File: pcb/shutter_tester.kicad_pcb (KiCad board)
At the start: 2 copper layers, 53 x 42 mm, 24 parts, among them J1 Conn_01x02, J2 Conn_01x02, J3 Conn_01x02, J4 Conn_01x02, Q1 MMBTA13LT3G, Q2 MMBTA13LT3G, Q3 MMBTA13LT3G, Q4 MMBTA13LT3G

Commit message: change to single light sensor
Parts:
- removed D2, D3, D4: LED, LED_THT:LED_D3.0mm
- removed J2, J3, J4: Conn_01x02, Connector_PinHeader_2.54mm:PinHeader_1x02_P2.54mm_Horizontal
- removed JP1, JP2, JP3: 0R, Resistor_SMD:R_1206_3216Metric
- removed Q2, Q3, Q4: MMBTA13LT3G, Package_TO_SOT_SMD:SOT-23
- removed R2, R3, R4: 2k, Resistor_SMD:R_0805_2012Metric_Pad1.20x1.40mm_HandSolder
- moved J1 25.8 mm to (135.6, 113.5), turned to 180 degrees
- moved R1 20.6 mm to (157.5, 117.8), turned to 180 degrees
- moved D1 17.8 mm to (158.8, 122.0), turned to 180 degrees
- moved Q1 16.4 mm to (152.3, 121.0)
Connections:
- J1 pad 1: Net-(J1-Pad1) -> GND
- J1 pad 2: GND -> Net-(J1-Pad2)
- Q1 pad 1: Net-(JP1-Pad1) -> Net-(D1-Pad2)
- Q1 pad 3: Net-(J1-Pad1) -> Net-(J1-Pad2)
- R1 pad 2: Net-(J1-Pad1) -> Net-(J1-Pad2)
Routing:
- net VCC: track 104.1 -> 28.1 mm
- net Net-(J1-Pad2): track 0.00 -> 29.7 mm
- net Net-(D3-Pad2): track 23.2 -> 0.00 mm
- net Net-(J4-Pad1): track 20.2 -> 0.00 mm
- net Net-(J3-Pad1): track 20.0 -> 0.00 mm
- net Net-(JP2-Pad1): track 10.3 -> 0.00 mm
- net Net-(J2-Pad1): track 8.12 -> 0.00 mm
- net Net-(J1-Pad1): track 8.12 -> 0.00 mm
- net Net-(JP1-Pad1): track 6.10 -> 0.00 mm
- net Net-(JP3-Pad1): track 4.83 -> 0.00 mm
- net Net-(D4-Pad2): track 4.41 -> 0.00 mm
- net Net-(D2-Pad2): track 4.23 -> 0.00 mm
- net Net-(D1-Pad2): track 5.16 -> 2.98 mm

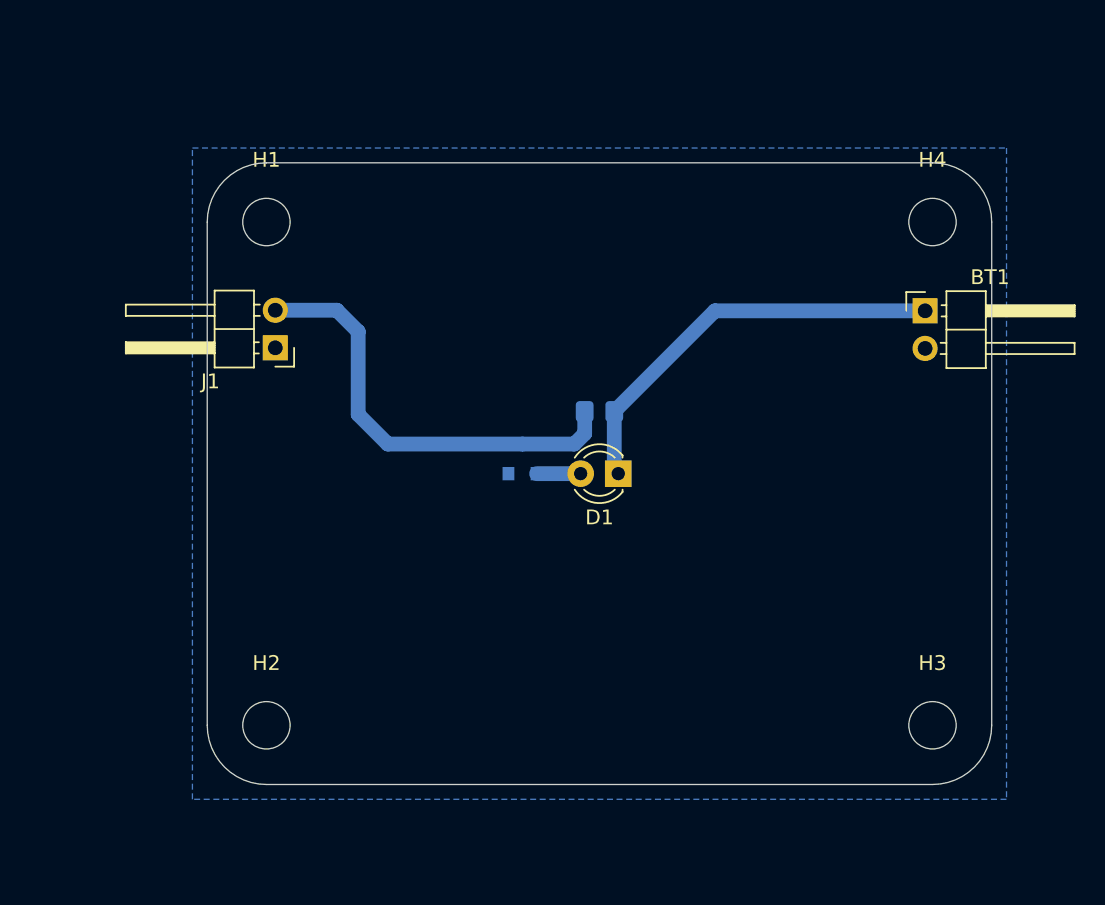
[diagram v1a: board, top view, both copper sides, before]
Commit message: add comparator circuit
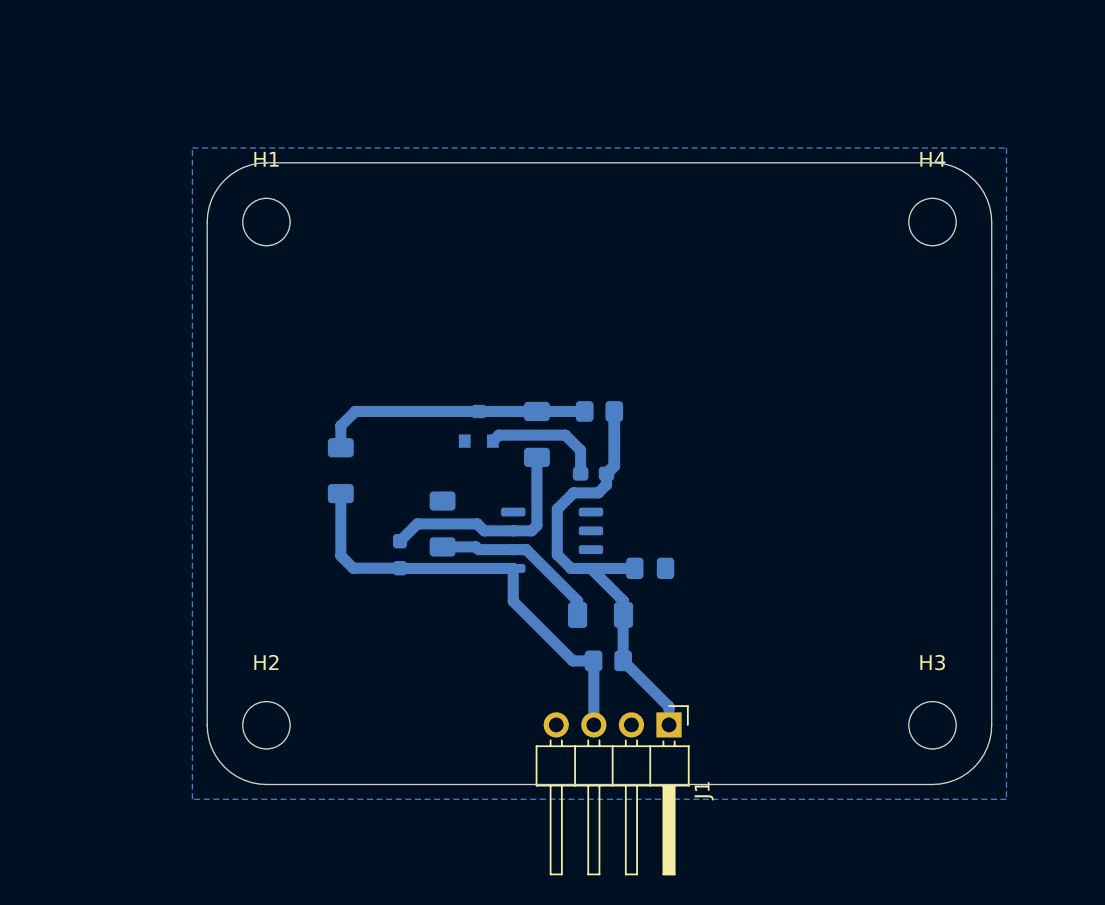
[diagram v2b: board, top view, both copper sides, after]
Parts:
- removed BT1: 2x AA, Connector_PinHeader_2.54mm:PinHeader_1x02_P2.54mm_Horizontal
- added C1: 100n, Capacitor_SMD:C_0805_2012Metric_Pad1.18x1.45mm_HandSolder, B.Cu at (160.9, 128.4)
- added JP1: Comparitor Bypass, Resistor_SMD:R_1206_3216Metric_Pad1.30x1.75mm_HandSolder, B.Cu at (140.0, 121.8)
- added R2: 10k, Resistor_SMD:R_1206_3216Metric_Pad1.30x1.75mm_HandSolder, B.Cu at (153.3, 119.3)
- added R3: 10k, Resistor_SMD:R_1206_3216Metric_Pad1.30x1.75mm_HandSolder, B.Cu at (157.6, 131.6)
- added R4: 10k, Resistor_SMD:R_1206_3216Metric_Pad1.30x1.75mm_HandSolder, B.Cu at (146.9, 125.4)
- added R5: 4.7M, Resistor_SMD:R_0603_1608Metric_Pad0.98x0.95mm_HandSolder, B.Cu at (144.0, 127.5)
- added R6: 3k, Resistor_SMD:R_0805_2012Metric_Pad1.20x1.40mm_HandSolder, B.Cu at (158.1, 134.7)
- added U1: LM393, Package_SO:SOP-8_3.9x4.9mm_P1.27mm, B.Cu at (154.3, 126.5)
- D1: footprint LED_THT:LED_D3.0mm -> LED_SMD:LED_0603_1608Metric_Pad1.05x0.95mm_HandSolder; moved to B.Cu
- J1: value Conn_01x02 -> Conn_01x04; footprint Connector_PinHeader_2.54mm:PinHeader_1x02_P2.54mm_Horizontal -> Connector_PinHeader_2.54mm:PinHeader_1x04_P2.54mm_Horizontal
- moved J1 36.8 mm to (162.2, 139.0), turned to 270 degrees
- moved Q1 3.68 mm to (149.3, 118.8)
- moved D1 1.67 mm to (157.1, 122.0)
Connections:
- J1 pad 1: GND -> VCC
- J1 pad 2: Net-(J1-Pad2) -> GND
- Q1 pad 3: Net-(J1-Pad2) -> Net-(JP1-Pad1)
- R1 pad 2: Net-(J1-Pad2) -> Net-(JP1-Pad1)
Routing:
- net /OUTPUT: track 0.00 -> 29.8 mm
- net Net-(J1-Pad2): track 29.7 -> 0.00 mm
- net Net-(JP1-Pad1): track 0.00 -> 18.4 mm
- net Net-(R2-Pad1): track 0.00 -> 14.7 mm
- net Net-(R3-Pad1): track 0.00 -> 11.6 mm
- net Net-(D1-Pad2): track 2.98 -> 8.09 mm
- net VCC: track 28.1 -> 30.7 mm

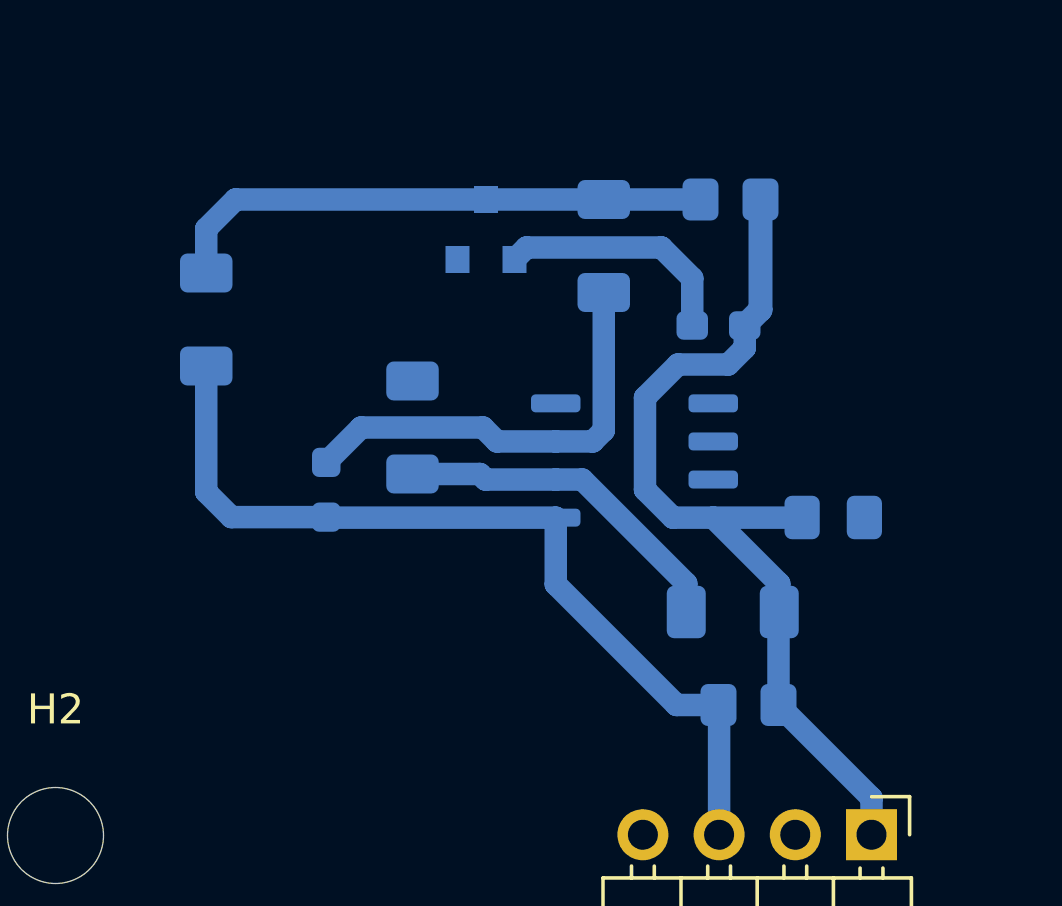
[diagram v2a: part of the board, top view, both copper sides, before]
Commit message: move tracks for engraving tip access
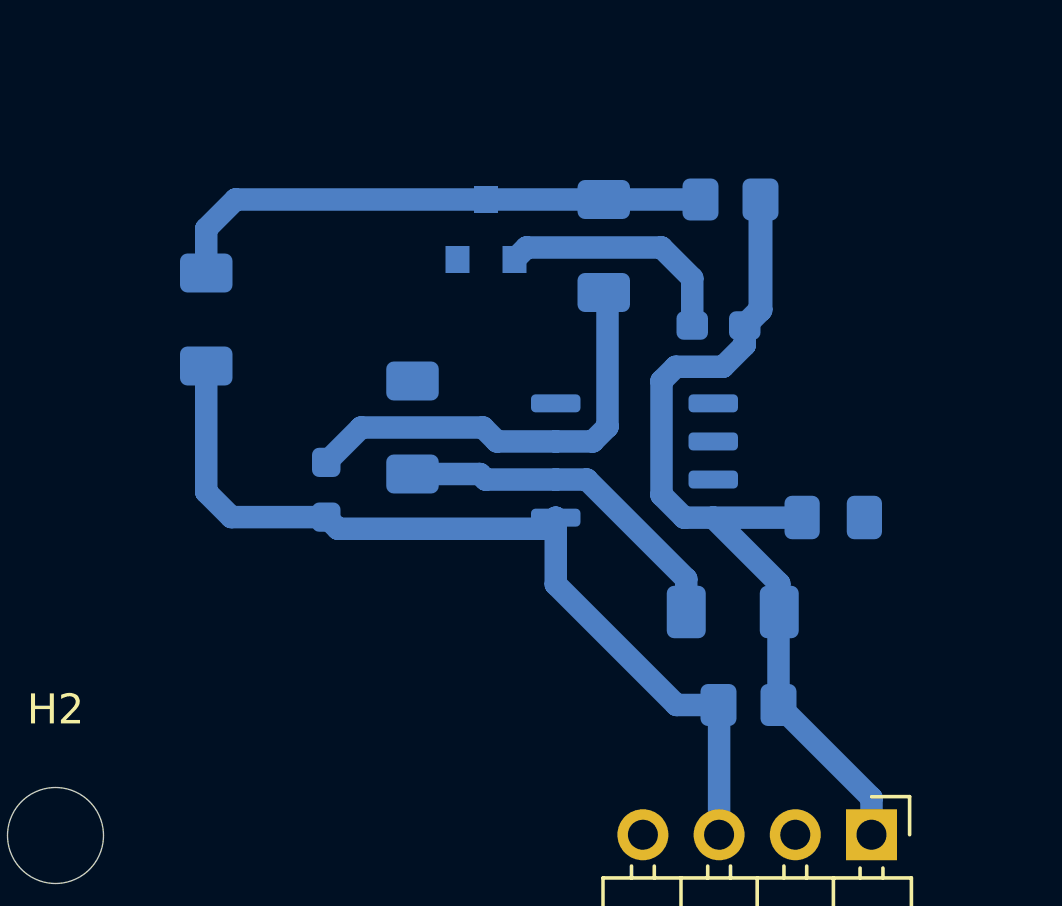
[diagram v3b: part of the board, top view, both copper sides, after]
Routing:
- net VCC: track 30.7 -> 29.9 mm
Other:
- net class Default: clearance 0.2 -> 0.4536
- rule trace_clearance: 0.2 -> 0.4536
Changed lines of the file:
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@@
     (thickness 1.6)
     (drawings 12)
-    (tracks 51)
+    (tracks 53)
     (zones 0)
     (modules 16)
@@
     (user_trace_width 0.8)
     (user_trace_width 1)
-    (trace_clearance 0.2)
+    (trace_clearance 0.4536)
     (zone_clearance 0.508)
     (zone_45_only yes)
@@
   (net 7 /OUTPUT)
   (net_class Default "This is the default net class."
-    (clearance 0.2)
+    (clearance 0.4536)
     (trace_width 0.25)
     (via_dia 0.8)
@@
     (fp_line (start 2.45 1.12) (end 2.45 -1.12) (layer B.CrtYd) (width 0.05))
     (fp_line (start 2.45 -1.12) (end -2.45 -1.12) (layer B.CrtYd) (width 0.05))
-    (pad 2 smd roundrect (at 1.55 0 270) (size 1.3 1.75) (layers B.Cu B.Paste B.Mask) (roundrect_rratio 0.192308)
+    (pad 2 smd roundrect (at 1.55 0 270) (size 1.3 1.75) (layers B.Cu B.Paste B.Mask) (roundrect_rratio 0.1923076923076923)
       (net 7 /OUTPUT))
-    (pad 1 smd roundrect (at -1.55 0 270) (size 1.3 1.75) (layers B.Cu B.Paste B.Mask) (roundrect_rratio 0.192308)
+    (pad 1 smd roundrect (at -1.55 0 270) (size 1.3 1.75) (layers B.Cu B.Paste B.Mask) (roundrect_rratio 0.1923076923076923)
       (net 4 "Net-(JP1-Pad1)"))
     (model ${KISYS3DMOD}/Resistor_SMD.3dshapes/R_1206_3216Metric.wrl
@@
     (fp_line (start 2.45 1.12) (end 2.45 -1.12) (layer B.CrtYd) (width 0.05))
     (fp_line (start 2.45 -1.12) (end -2.45 -1.12) (layer B.CrtYd) (width 0.05))
-    (pad 2 smd roundrect (at 1.55 0 90) (size 1.3 1.75) (layers B.Cu B.Paste B.Mask) (roundrect_rratio 0.192308)
+    (pad 2 smd roundrect (at 1.55 0 90) (size 1.3 1.75) (layers B.Cu B.Paste B.Mask) (roundrect_rratio 0.1923076923076923)
       (net 4 "Net-(JP1-Pad1)"))
-    (pad 1 smd roundrect (at -1.55 0 90) (size 1.3 1.75) (layers B.Cu B.Paste B.Mask) (roundrect_rratio 0.192308)
+    (pad 1 smd roundrect (at -1.55 0 90) (size 1.3 1.75) (layers B.Cu B.Paste B.Mask) (roundrect_rratio 0.1923076923076923)
       (net 5 "Net-(R2-Pad1)"))
     (model ${KISYS3DMOD}/Resistor_SMD.3dshapes/R_1206_3216Metric.wrl
@@
       (effects (font (size 0.8 0.8) (thickness 0.12)) (justify mirror))
     )
-    (pad 2 smd roundrect (at 1.55 0 270) (size 1.3 1.75) (layers B.Cu B.Paste B.Mask) (roundrect_rratio 0.192308)
+    (pad 2 smd roundrect (at 1.55 0 270) (size 1.3 1.75) (layers B.Cu B.Paste B.Mask) (roundrect_rratio 0.1923076923076923)
       (net 6 "Net-(R3-Pad1)"))
-    (pad 1 smd roundrect (at -1.55 0 270) (size 1.3 1.75) (layers B.Cu B.Paste B.Mask) (roundrect_rratio 0.192308)
+    (pad 1 smd roundrect (at -1.55 0 270) (size 1.3 1.75) (layers B.Cu B.Paste B.Mask) (roundrect_rratio 0.1923076923076923)
       (net 1 GND))
     (model ${KISYS3DMOD}/Resistor_SMD.3dshapes/R_1206_3216Metric.wrl
@@
       (effects (font (size 0.8 0.8) (thickness 0.12)) (justify mirror))
     )
-    (pad 2 smd roundrect (at 1.55 0) (size 1.3 1.75) (layers B.Cu B.Paste B.Mask) (roundrect_rratio 0.192308)
+    (pad 2 smd roundrect (at 1.55 0) (size 1.3 1.75) (layers B.Cu B.Paste B.Mask) (roundrect_rratio 0.1923076923076923)
       (net 2 VCC))
-    (pad 1 smd roundrect (at -1.55 0) (size 1.3 1.75) (layers B.Cu B.Paste B.Mask) (roundrect_rratio 0.192308)
+    (pad 1 smd roundrect (at -1.55 0) (size 1.3 1.75) (layers B.Cu B.Paste B.Mask) (roundrect_rratio 0.1923076923076923)
       (net 6 "Net-(R3-Pad1)"))
     (model ${KISYS3DMOD}/Resistor_SMD.3dshapes/R_1206_3216Metric.wrl
@@
       (effects (font (size 0.5 0.5) (thickness 0.08)) (justify mirror))
     )
-    (pad 2 smd roundrect (at 1.0375 0) (size 1.175 1.45) (layers B.Cu B.Paste B.Mask) (roundrect_rratio 0.212766)
-      (net 1 GND))
-    (pad 1 smd roundrect (at -1.0375 0) (size 1.175 1.45) (layers B.Cu B.Paste B.Mask) (roundrect_rratio 0.212766)
+    (pad 2 smd roundrect (at 1.0375 0) (size 1.175 1.45) (layers B.Cu B.Paste B.Mask) (roundrect_rratio 0.2127659574468085)
+      (net 1 GND))
+    (pad 1 smd roundrect (at -1.0375 0) (size 1.175 1.45) (layers B.Cu B.Paste B.Mask) (roundrect_rratio 0.2127659574468085)
       (net 2 VCC))
     (model ${KISYS3DMOD}/Capacitor_SMD.3dshapes/C_0805_2012Metric.wrl
@@
       (effects (font (size 0.5 0.5) (thickness 0.08)) (justify mirror))
     )
-    (pad 2 smd roundrect (at 1 0) (size 1.2 1.4) (layers B.Cu B.Paste B.Mask) (roundrect_rratio 0.208333)
+    (pad 2 smd roundrect (at 1 0) (size 1.2 1.4) (layers B.Cu B.Paste B.Mask) (roundrect_rratio 0.2083325)
       (net 2 VCC))
-    (pad 1 smd roundrect (at -1 0) (size 1.2 1.4) (layers B.Cu B.Paste B.Mask) (roundrect_rratio 0.208333)
+    (pad 1 smd roundrect (at -1 0) (size 1.2 1.4) (layers B.Cu B.Paste B.Mask) (roundrect_rratio 0.2083325)
       (net 7 /OUTPUT))
     (model ${KISYS3DMOD}/Resistor_SMD.3dshapes/R_0805_2012Metric.wrl
@@
   (segment (start 159.8825 128.405) (end 159.8875 128.4) (width 0.75) (layer B.Cu) (net 2))
   (segment (start 156.925 128.405) (end 159.8825 128.405) (width 0.75) (layer B.Cu) (net 2))
-  (segment (start 157.975 122.75) (end 157.975 122) (width 0.75) (layer B.Cu) (net 2))
-  (segment (start 157.425 123.3) (end 157.975 122.75) (width 0.75) (layer B.Cu) (net 2))
-  (segment (start 154.65 124.4) (end 155.75 123.3) (width 0.75) (layer B.Cu) (net 2))
-  (segment (start 154.65 127.475) (end 154.65 124.4) (width 0.75) (layer B.Cu) (net 2))
-  (segment (start 155.75 123.3) (end 157.425 123.3) (width 0.75) (layer B.Cu) (net 2))
-  (segment (start 155.58 128.405) (end 154.65 127.475) (width 0.75) (layer B.Cu) (net 2))
-  (segment (start 156.925 128.405) (end 155.58 128.405) (width 0.75) (layer B.Cu) (net 2))
   (segment (start 162.2 137.75) (end 159.1 134.65) (width 0.75) (layer B.Cu) (net 2))
   (segment (start 162.2 138.975) (end 162.2 137.75) (width 0.75) (layer B.Cu) (net 2))
@@
   (segment (start 159.125 130.605) (end 156.925 128.405) (width 0.75) (layer B.Cu) (net 2))
   (segment (start 159.125 131.55) (end 159.125 130.605) (width 0.75) (layer B.Cu) (net 2))
+  (segment (start 157.25 123.375) (end 157.975 122.65) (width 0.75) (layer B.Cu) (net 2))
+  (segment (start 155.675 123.375) (end 157.25 123.375) (width 0.75) (layer B.Cu) (net 2))
+  (segment (start 155.2 123.85) (end 155.675 123.375) (width 0.75) (layer B.Cu) (net 2))
+  (segment (start 155.2 127.65) (end 155.2 123.85) (width 0.75) (layer B.Cu) (net 2))
+  (segment (start 155.955 128.405) (end 155.2 127.65) (width 0.75) (layer B.Cu) (net 2))
+  (segment (start 157.975 122.65) (end 157.975 122) (width 0.75) (layer B.Cu) (net 2))
+  (segment (start 156.925 128.405) (end 155.955 128.405) (width 0.75) (layer B.Cu) (net 2))
   (segment (start 156.225 122) (end 156.225 120.425) (width 0.75) (layer B.Cu) (net 3))
   (segment (start 156.225 120.425) (end 155.2 119.4) (width 0.75) (layer B.Cu) (net 3))
   (segment (start 150.7 119.4) (end 150.3 119.8) (width 0.75) (layer B.Cu) (net 3))
   (segment (start 155.2 119.4) (end 150.7 119.4) (width 0.75) (layer B.Cu) (net 3))
-  (segment (start 151.675 125.865) (end 152.91 125.865) (width 0.75) (layer B.Cu) (net 5))
-  (segment (start 153.275 125.5) (end 153.275 120.9) (width 0.75) (layer B.Cu) (net 5))
-  (segment (start 152.91 125.865) (end 153.275 125.5) (width 0.75) (layer B.Cu) (net 5))
-  (segment (start 144.0425 128.405) (end 144.025 128.3875) (width 0.75) (layer B.Cu) (net 7))
-  (segment (start 151.675 128.405) (end 144.0425 128.405) (width 0.75) (layer B.Cu) (net 7))
   (segment (start 157.12 134.67) (end 157.1 134.65) (width 0.75) (layer B.Cu) (net 7))
   (segment (start 157.12 138.975) (end 157.12 134.67) (width 0.75) (layer B.Cu) (net 7))
@@
   (segment (start 145.1875 125.4) (end 149.25 125.4) (width 0.75) (layer B.Cu) (net 5))
   (segment (start 144.025 126.5625) (end 145.1875 125.4) (width 0.75) (layer B.Cu) (net 5))
+  (segment (start 153.4 121.025) (end 153.275 120.9) (width 0.75) (layer B.Cu) (net 5))
+  (segment (start 153.4 125.375) (end 153.4 121.025) (width 0.75) (layer B.Cu) (net 5))
+  (segment (start 152.91 125.865) (end 153.4 125.375) (width 0.75) (layer B.Cu) (net 5))
+  (segment (start 151.675 125.865) (end 152.91 125.865) (width 0.75) (layer B.Cu) (net 5))
   (segment (start 151.675 127.135) (end 149.335 127.135) (width 0.75) (layer B.Cu) (net 6))
   (segment (start 149.15 126.95) (end 146.9 126.95) (width 0.75) (layer B.Cu) (net 6))
   (segment (start 149.335 127.135) (end 149.15 126.95) (width 0.75) (layer B.Cu) (net 6))
   (segment (start 156.025 131.475) (end 156.025 131.55) (width 0.75) (layer B.Cu) (net 6))
-  (segment (start 156.025 130.6) (end 156.025 131.475) (width 0.75) (layer B.Cu) (net 6))
-  (segment (start 152.56 127.135) (end 156.025 130.6) (width 0.75) (layer B.Cu) (net 6))
-  (segment (start 151.675 127.135) (end 152.56 127.135) (width 0.75) (layer B.Cu) (net 6))
+  (segment (start 156.025 130.45) (end 156.025 131.475) (width 0.75) (layer B.Cu) (net 6))
+  (segment (start 152.71 127.135) (end 156.025 130.45) (width 0.75) (layer B.Cu) (net 6))
+  (segment (start 151.675 127.135) (end 152.71 127.135) (width 0.75) (layer B.Cu) (net 6))
   (segment (start 144.025 128.3875) (end 140.8625 128.3875) (width 0.75) (layer B.Cu) (net 7))
   (segment (start 140.025 127.55) (end 140.025 123.35) (width 0.75) (layer B.Cu) (net 7))
@@
   (segment (start 151.675 130.625) (end 151.675 128.405) (width 0.75) (layer B.Cu) (net 7))
   (segment (start 157.1 134.65) (end 155.7 134.65) (width 0.75) (layer B.Cu) (net 7))
+  (segment (start 144.4125 128.775) (end 144.025 128.3875) (width 0.75) (layer B.Cu) (net 7))
+  (segment (start 151.305 128.775) (end 144.4125 128.775) (width 0.75) (layer B.Cu) (net 7))
+  (segment (start 151.675 128.405) (end 151.305 128.775) (width 0.75) (layer B.Cu) (net 7))
   (zone (net 1) (net_name GND) (layer B.Cu) (hatch edge 0.508)
     (connect_pads (clearance 0.508))
